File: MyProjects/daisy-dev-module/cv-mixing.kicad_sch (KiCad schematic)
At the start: 65 parts, among them J10 CV_IN_6, J11 CV_IN_7, J12 CV_IN_8, J5 CV_IN_1, J6 CV_IN_2, J7 CV_IN_3, J8 CV_IN_4, J9 CV_IN_5, U4 MCP6004, U5 MCP6004, U6 LM4040DBZ-10

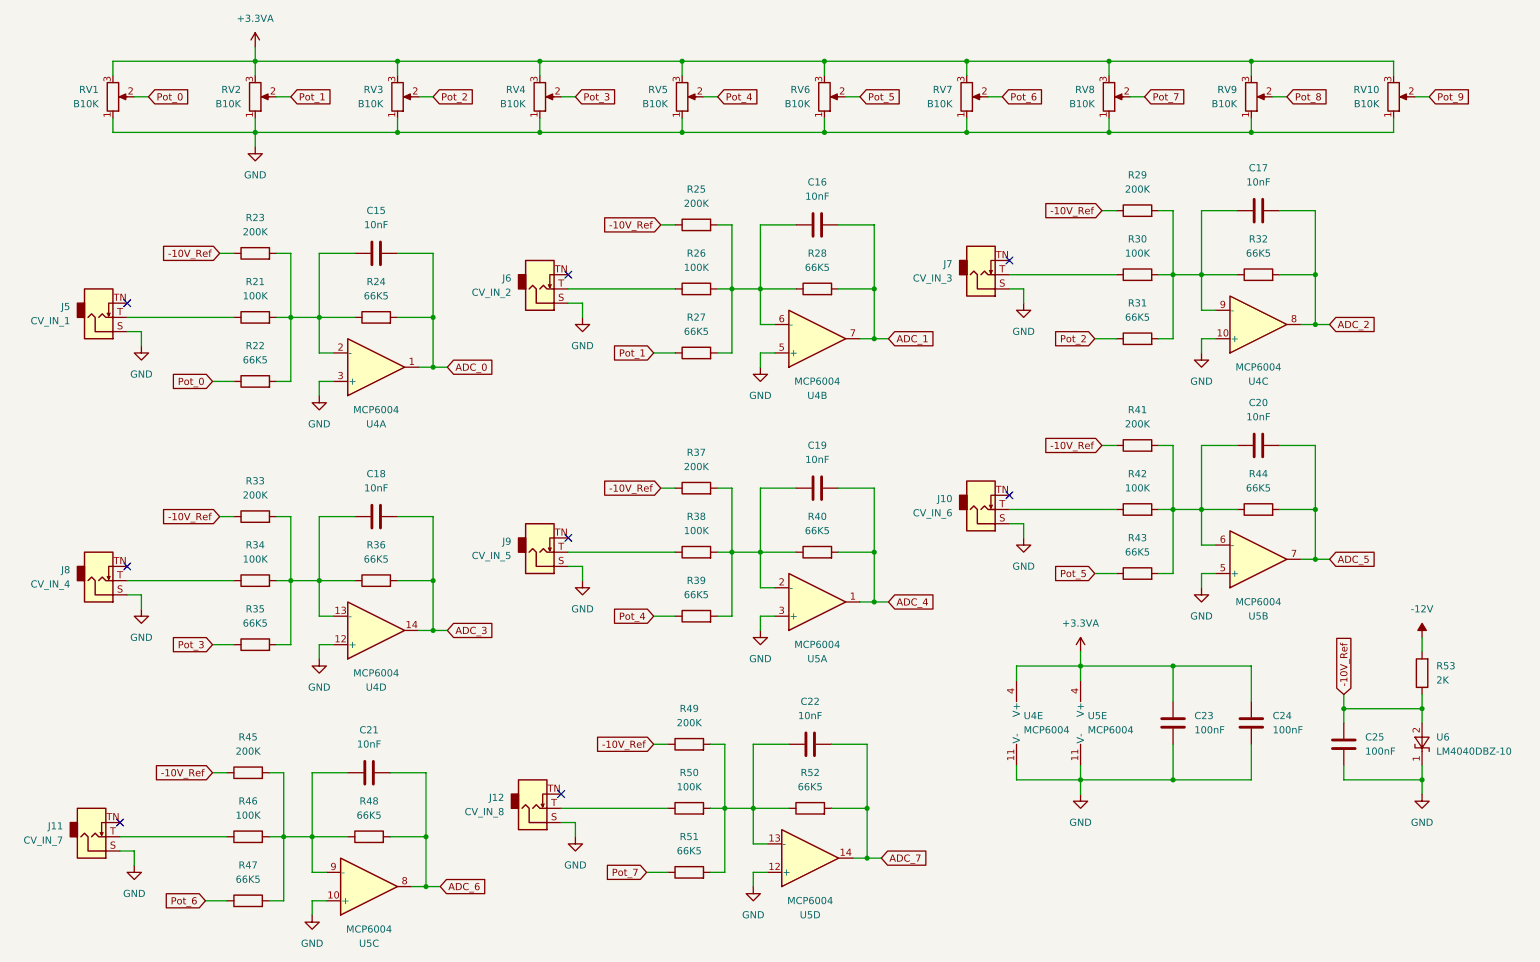
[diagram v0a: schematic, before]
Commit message: Update delay-module.cpp
Add encoder (does nothing right now) and remove one LED.
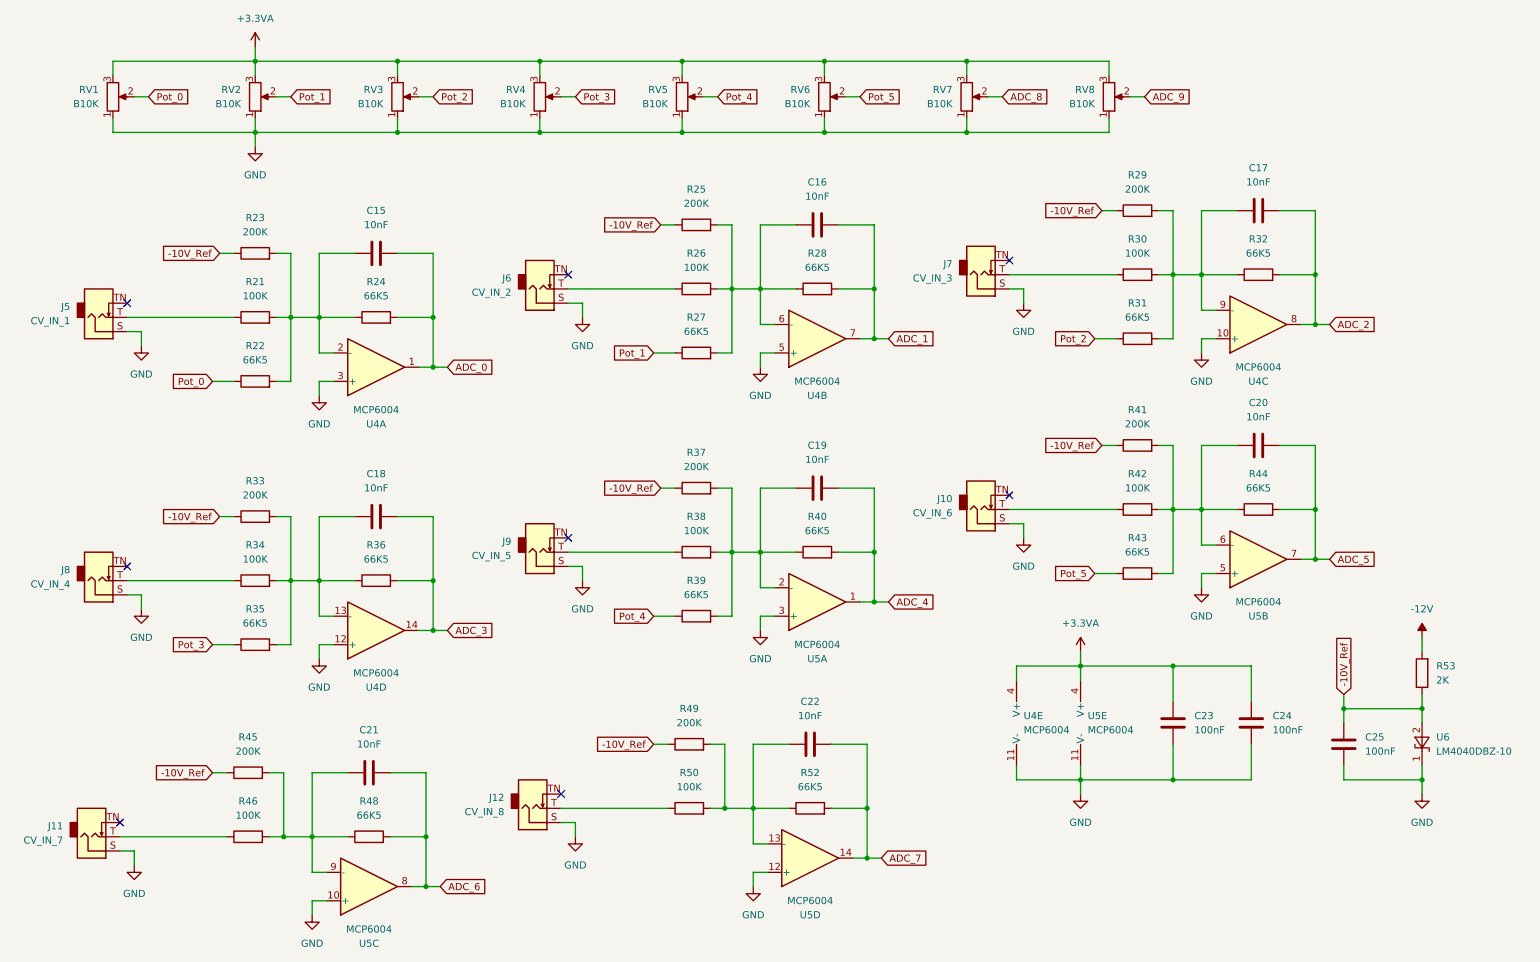
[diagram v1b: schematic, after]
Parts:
- removed R47, R51: 66K5, Resistor_SMD:R_0805_2012Metric_Pad1.20x1.40mm_HandSolder, symbol Device:R
- removed RV10, RV9: B10K, Potentiometer_THT:Potentiometer_Alpha_RD901F-40-00D_Single_Vertical_CircularHoles, symbol Device:R_Potentiometer
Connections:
- net Pot_6 renamed ADC_8
- net Pot_7 renamed ADC_9
